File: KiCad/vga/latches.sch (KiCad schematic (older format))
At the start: 7 parts, among them U12 74AC573, U13 74AC573, U15 74AC573, U16 74AC573, U17 74AC245, U18 27C512, U19 74AC151

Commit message: Updated graphics adapter and main schematics + board.
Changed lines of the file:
@@
 Text Notes 7750 3650 0    50   ~ 0
 character ROM
-Text Notes 9300 3250 0    50   ~ 0
+Text Notes 9200 3250 0    50   ~ 0
 8:1 multiplexer
 Wire Bus Line

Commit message: Updated graphics adapter
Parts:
- removed U19: 74AC151, Package_DIP:DIP-16_W7.62mm_LongPads, symbol 74xx:74LS151
- added U19: 74AC166, Package_DIP:DIP-16_W7.62mm_LongPads, symbol 74xx:74LS166
- U17: value 74AC245 -> 74HC245
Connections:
- net labels added: LATCH_CHR, LATCH_COL, PX_CLK, ~PE_CHPX
- net labels removed: CHCOL0, CHCOL1, CHCOL2, LATCH
- wire segments 121 -> 126
- no-connect marks 1 -> 0
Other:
- note removed: "8:1 multiplexer"
- moved on the sheet: U13, U16

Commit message: Replaced MAX7000 CPLD with MAX II in graphics adapter. PCB redesign with smaller size.
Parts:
- U17: value 74HC245 -> 74AC245
- U19: value 74AC166 -> 74F166
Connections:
- net at U19.10 (E): now also U18.15 (D3); no longer U18.16 (D4)
- net at U19.11 (F): now also U18.13 (D2); no longer U18.17 (D5)
- net at U19.12 (G): now also U18.12 (D1); no longer U18.18 (D6)
- net at U19.14 (H): now also U18.11 (D0); no longer U18.19 (D7)
- net at U19.2 (A): now also U18.19 (D7); no longer U18.11 (D0)
- net at U19.3 (B): now also U18.18 (D6); no longer U18.12 (D1)
- net at U19.4 (C): now also U18.17 (D5); no longer U18.13 (D2)
- net at U19.5 (D): now also U18.16 (D4); no longer U18.15 (D3)
- net ~CHARPIXEL renamed CHARPIXEL
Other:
- moved on the sheet: U18, U19

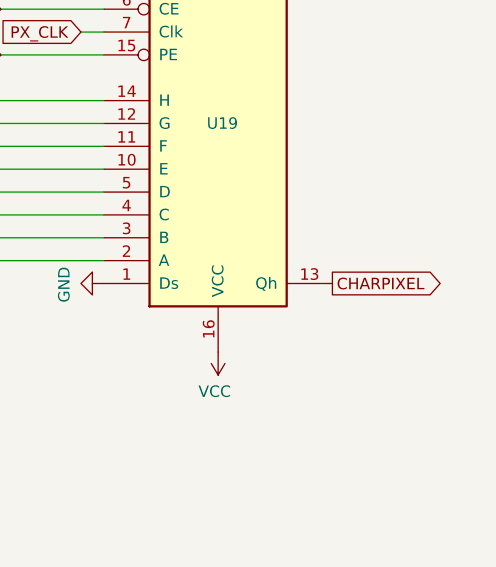
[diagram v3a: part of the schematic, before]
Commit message: Finished VGA adapter Rev. 1.0
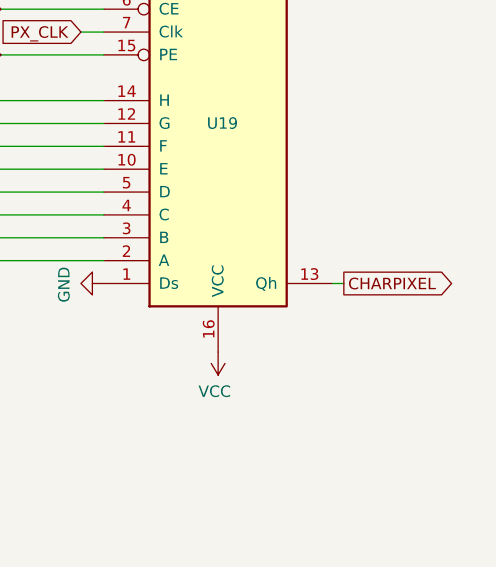
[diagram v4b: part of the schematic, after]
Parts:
- U19: footprint Package_DIP:DIP-16_W7.62mm_LongPads -> Package_DIP:DIP-16_W7.62mm_Socket_LongPads
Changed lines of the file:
@@
 Text GLabel 7100 4500 0    50   Input ~ 0
 ~CHARMODE
-Text GLabel 10250 3600 2    50   Output ~ 0
+Text GLabel 10300 3600 2    50   Output ~ 0
 CHARPIXEL
 Wire Bus Line
@@
 F 0 "U19" H 9700 2900 50  0000 L CNN
 F 1 "74F166" H 9850 2000 50  0000 L CNN
-F 2 "Package_DIP:DIP-16_W7.62mm_LongPads" H 9750 2900 50  0001 C CNN
+F 2 "Package_DIP:DIP-16_W7.62mm_Socket_LongPads" H 9750 2900 50  0001 C CNN
 F 3 "http://www.ti.com/lit/gpn/sn74LS166" H 9750 2900 50  0001 C CNN
 	1    9750 2900
@@
 Wire Wire Line
 	9250 2400 8800 2400
+Wire Wire Line
+	10250 3600 10300 3600
 Wire Bus Line
 	6850 800  6850 3800
